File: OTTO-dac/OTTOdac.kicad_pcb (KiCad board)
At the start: 2 copper layers, 73 x 35 mm, 40 parts, among them J1 Conn_01x10, J2 Audio_IN, J3 Audio_OUT, J4 SJ1-42536-SMT, J5 Speaker, U1 AMS1117-3.3, U2 SGTL5000, U3 LM4860, X1 XO32

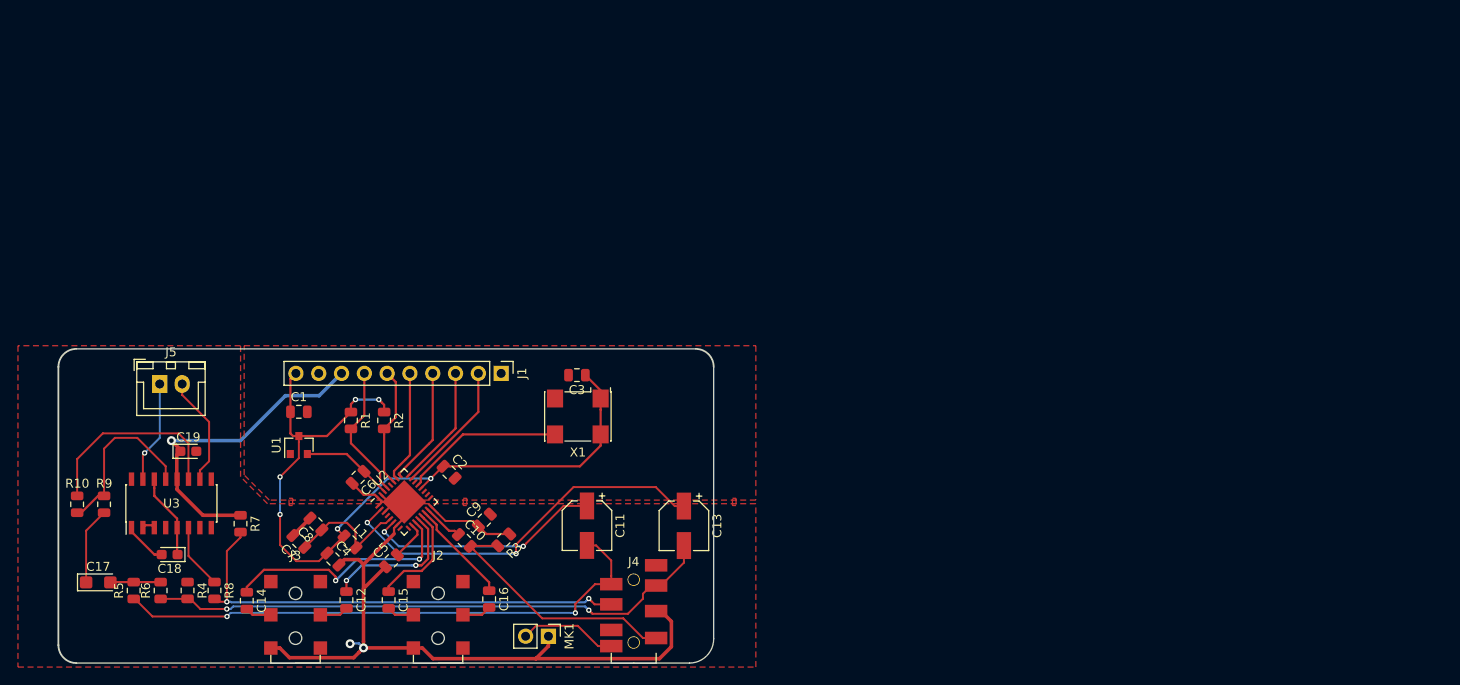
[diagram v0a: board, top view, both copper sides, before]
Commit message: new board, still needs gnd to be routed
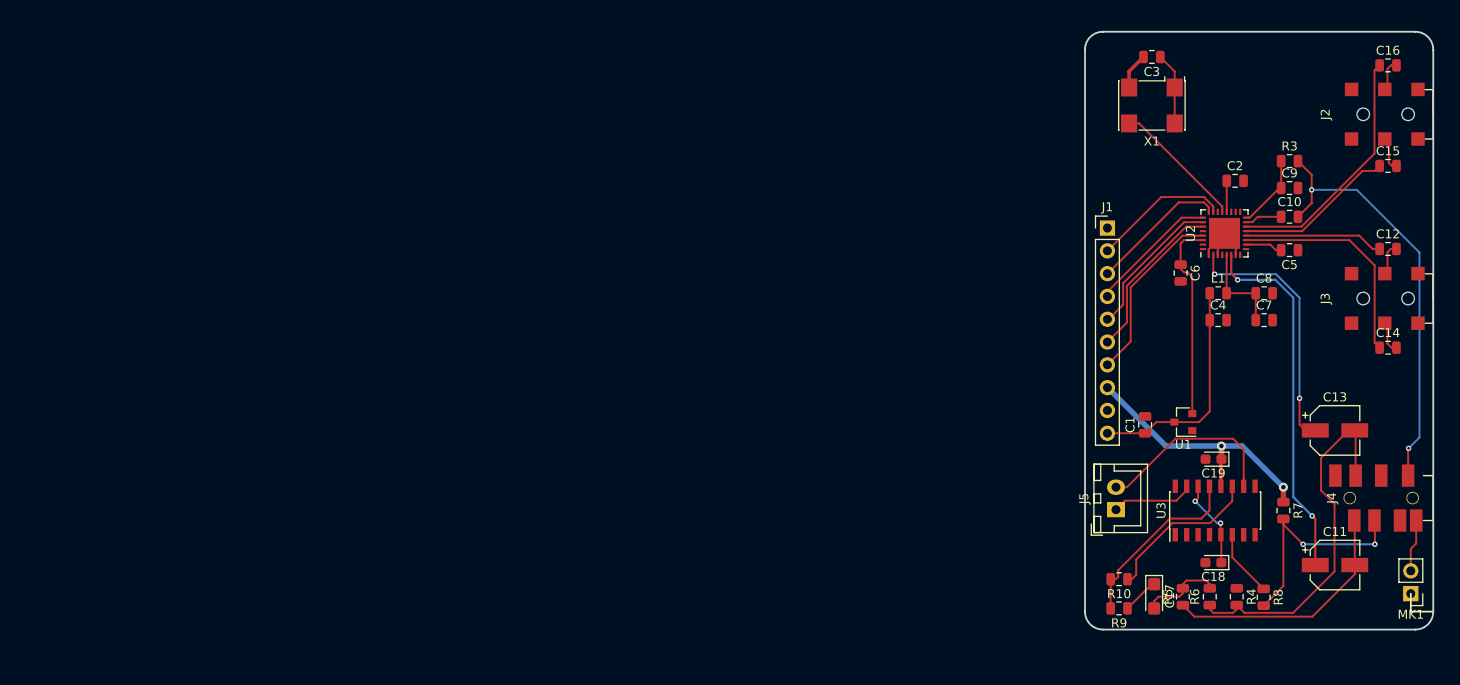
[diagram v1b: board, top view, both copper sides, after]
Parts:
- removed R1, R2: 2.2K, Resistor_SMD:R_0805_2012Metric
- moved C14 130.2 mm to (328.2, 118.6), turned to 0 degrees
- moved J3 128.1 mm to (329.2, 113.1), turned to 270 degrees
- moved C12 122.4 mm to (328.2, 107.6), turned to 0 degrees
- moved C15 121.4 mm to (328.2, 98.4), turned to 0 degrees
- moved J2 121.2 mm to (329.2, 92.6), turned to 270 degrees
- moved C17 117.6 mm to (302.1, 146.3), turned to 270 degrees
- moved R8 116.9 mm to (314.3, 146.4)
- moved R4 116.9 mm to (311.3, 146.4)
- moved R5 116.9 mm to (305.3, 146.4)
- moved R6 116.9 mm to (308.3, 146.4)
- moved C16 116.5 mm to (328.2, 87.2), turned to 0 degrees
- moved R10 116.4 mm to (298.2, 144.4), turned to 180 degrees
- moved C18 116.3 mm to (308.7, 142.6)
- moved U3 116.3 mm to (308.9, 136.8)
- moved R7 116.2 mm to (316.5, 136.8)
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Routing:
- net GNDREF: track 103.7 -> 9.25 mm, vias 2 -> 0
- net +3V3: track 87.1 -> 37.1 mm, vias 6 -> 0
- net HPL: track 62.0 -> 27.6 mm, vias 2 -> 0
- net Net-(J4-Pad6): track 53.2 -> 25.0 mm
- net HPR: track 63.5 -> 40.8 mm, vias 2 -> 0
- net MIC: track 28.0 -> 47.7 mm, vias 0 -> 2
- net Net-(C16-Pad1): track 11.7 -> 27.7 mm
- net Net-(C11-Pad1): track 26.7 -> 41.5 mm
- net Net-(C13-Pad1): track 43.4 -> 28.9 mm
- net Net-(C6-Pad1): track 10.1 -> 22.4 mm
- net Net-(J5-Pad2): track 12.3 -> 21.1 mm
- net +5V: track 36.3 -> 30.4 mm, vias 1 -> 2
- net Net-(C15-Pad1): track 12.2 -> 17.9 mm
- net Net-(J4-Pad8): track 11.0 -> 5.86 mm
- net PIN5: track 15.1 -> 20.1 mm
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- removed copper zone on F.Cu, net GNDREF
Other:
- board size 73 x 35 mm -> 38.8 x 66.6 mm

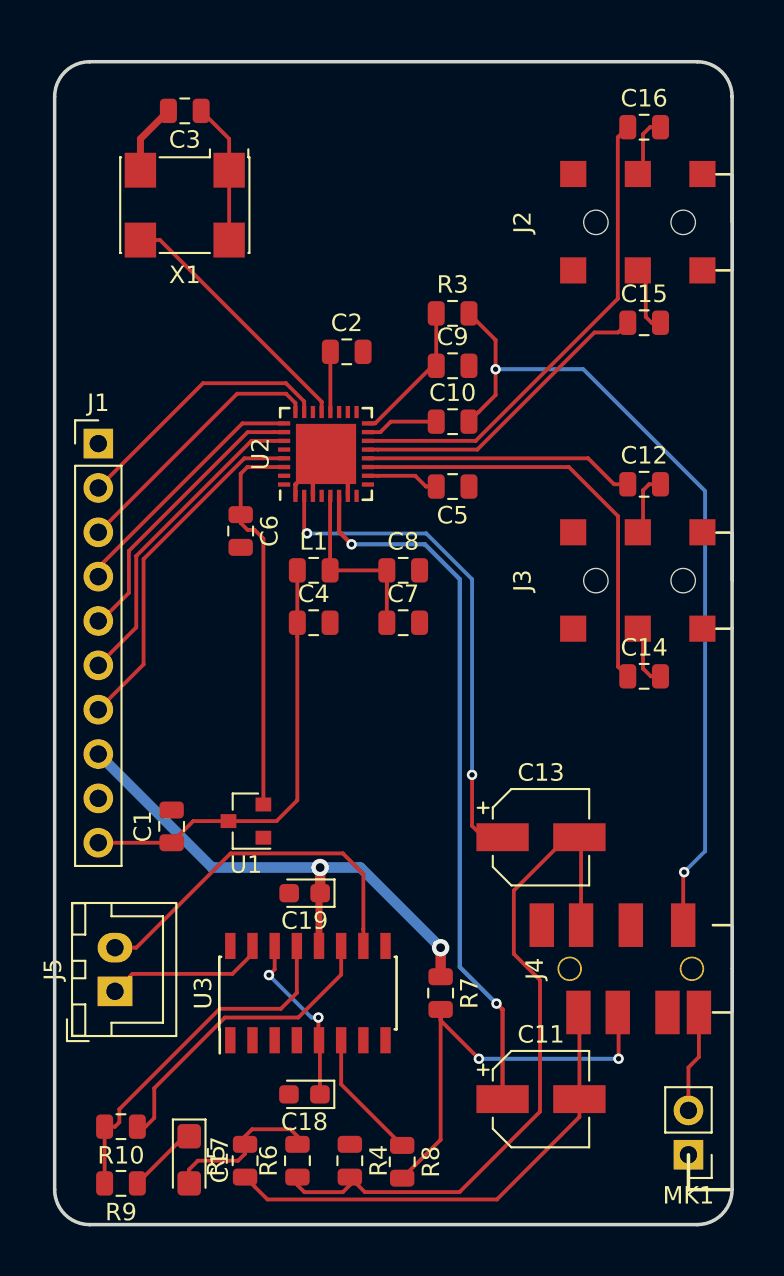
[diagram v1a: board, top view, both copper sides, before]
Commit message: routed ground and added mounting holes
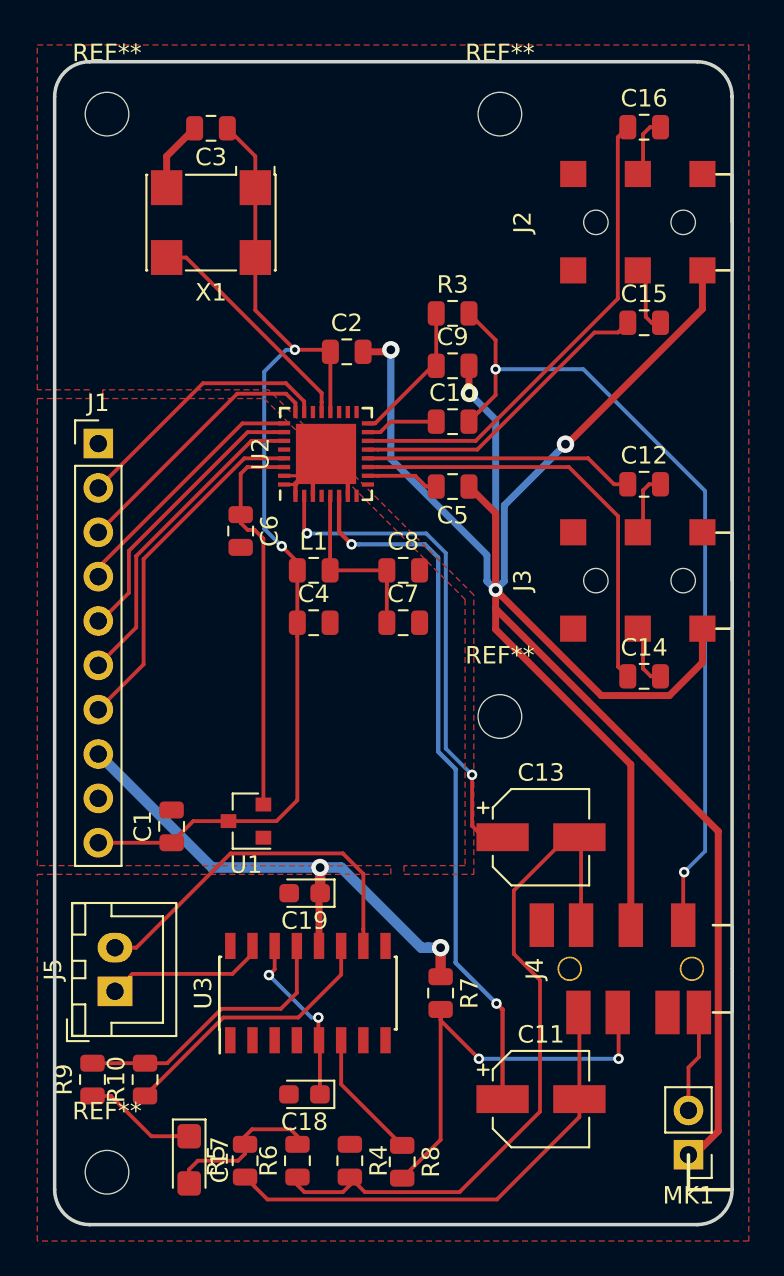
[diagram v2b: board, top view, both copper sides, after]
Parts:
- added REF**: MountingHole_2.5mm, MountingHole:MountingHole_2.5mm, F.Cu at (297.4, 147.0)
- added REF**: MountingHole_2.5mm, MountingHole:MountingHole_2.5mm, F.Cu at (319.9, 120.9)
- added REF**: MountingHole_2.5mm, MountingHole:MountingHole_2.5mm, F.Cu at (319.9, 86.4)
- added REF**: MountingHole_2.5mm, MountingHole:MountingHole_2.5mm, F.Cu at (297.4, 86.4)
- moved R9 6.17 mm to (296.6, 141.7), turned to 90 degrees
- moved R10 3.03 mm to (299.6, 141.7), turned to 90 degrees
- moved C3 1.80 mm to (303.4, 87.2)
- moved X1 1.80 mm to (303.4, 92.6)
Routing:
- net GNDREF: track 9.25 -> 157.9 mm, vias 0 -> 4
- net +3V3: track 37.1 -> 59.8 mm, vias 0 -> 2
- net Net-(R10-Pad2): track 20.6 -> 16.6 mm
- net Net-(C17-Pad1): track 4.09 -> 6.76 mm
- net Net-(R10-Pad1): track 17.9 -> 15.8 mm
- net Net-(U2-Pad21): track 14.8 -> 13.2 mm
- added copper zone on F.Cu, net GNDREF

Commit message: started working on the mainboard
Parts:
- moved MK1 1.30 mm to (329.4, 146.0)
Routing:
- net GNDREF: track 157.9 -> 159.2 mm
- net Net-(J4-Pad8): track 5.86 -> 6.40 mm
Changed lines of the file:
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@@
   (general
     (thickness 1.6)
-    (drawings 1356)
+    (drawings 1354)
     (tracks 304)
     (zones 0)
@@
     (pad_to_mask_clearance 0)
     (aux_axis_origin 0 0)
-    (grid_origin 294.428234 85.423074)
+    (grid_origin 329.428234 146.02262)
     (visible_elements 7FFFFFFF)
     (pcbplotparams
@@
   )
   (module Connector_PinHeader_2.54mm:PinHeader_1x02_P2.54mm_Vertical (layer F.Cu)
-    (at 330.726868 146.02262 180)
+    (at 329.428234 146.02262 180)
     (descr "Through hole straight pin header, 1x02, 2.54mm pitch, single row")
     (tags "Through hole pin header THT 1x02 2.54mm single row")
@@
   (gr_line (start 294.428234 86.423074) (end 296.928234 86.423074) (layer Cmts.User) (width 0.2))
   (gr_line (start 294.428234 85.423074) (end 294.428234 86.423074) (layer Cmts.User) (width 0.2))
-  (gr_line (start 330.726868 148.02262) (end 330.726868 146.02262) (layer F.SilkS) (width 0.2))
-  (gr_line (start 333.226868 148.02262) (end 330.726868 148.02262) (layer F.SilkS) (width 0.2))
   (gr_line (start 264.726868 169.58094) (end 274.726868 169.58094) (layer Cmts.User) (width 0.2))
   (gr_arc (start 273.726868 159.58094) (end 274.726868 159.58094) (angle -90) (layer Cmts.User) (width 0.2))
@@
   (segment (start 323.683869 105.326548) (end 320.183869 108.826548) (width 0.4) (layer B.Cu) (net 1))
   (segment (start 320.183869 108.826548) (end 320.183869 113.170762) (width 0.4) (layer B.Cu) (net 1))
-  (segment (start 328.183869 123.25) (end 319.683869 114.75) (width 0.4) (layer F.Cu) (net 1))
-  (segment (start 332.433869 127.5) (end 328.183869 123.25) (width 0.4) (layer F.Cu) (net 1))
-  (segment (start 332.433869 144.670782) (end 332.433869 127.5) (width 0.4) (layer F.Cu) (net 1))
-  (segment (start 330.726868 146.02262) (end 331.082031 146.02262) (width 0.4) (layer F.Cu) (net 1))
-  (segment (start 331.082031 146.02262) (end 332.433869 144.670782) (width 0.4) (layer F.Cu) (net 1))
   (segment (start 308.719713 107.136548) (end 309.107213 106.749048) (width 0.18) (layer F.Cu) (net 1))
   (segment (start 307.569713 107.136548) (end 308.719713 107.136548) (width 0.18) (layer F.Cu) (net 1))
@@
   (segment (start 310.832213 105.024048) (end 310.832213 106.749048) (width 0.18) (layer F.Cu) (net 1))
   (segment (start 309.107213 106.749048) (end 310.832213 106.749048) (width 0.18) (layer F.Cu) (net 1))
+  (segment (start 328.183869 123.25) (end 319.683869 114.75) (width 0.4) (layer F.Cu) (net 1))
+  (segment (start 332.433869 127.5) (end 328.183869 123.25) (width 0.4) (layer F.Cu) (net 1))
+  (segment (start 332.433869 144.670782) (end 332.433869 127.5) (width 0.4) (layer F.Cu) (net 1))
+  (segment (start 329.428234 146.023074) (end 331.081577 146.023074) (width 0.4) (layer F.Cu) (net 1))
+  (segment (start 331.081577 146.023074) (end 332.433869 144.670782) (width 0.4) (layer F.Cu) (net 1))
   (segment (start 309.568868 131.105259) (end 309.633869 131.040258) (width 0.4) (layer F.Cu) (net 2))
   (segment (start 309.568868 134.062757) (end 309.568868 131.105259) (width 0.4) (layer F.Cu) (net 2))
@@
   (segment (start 326.726868 137.92263) (end 326.676708 137.87247) (width 0.22) (layer F.Cu) (net 32))
   (segment (start 326.726868 140.52262) (end 326.726868 137.92263) (width 0.22) (layer F.Cu) (net 32))
-  (segment (start 330.726868 143.48262) (end 330.726868 141.02262) (width 0.22) (layer F.Cu) (net 34))
-  (segment (start 331.326708 140.42278) (end 331.326708 137.87247) (width 0.22) (layer F.Cu) (net 34))
-  (segment (start 330.726868 141.02262) (end 331.326708 140.42278) (width 0.22) (layer F.Cu) (net 34))
+  (segment (start 329.428234 142.321254) (end 329.428234 143.48262) (width 0.22) (layer F.Cu) (net 34))
+  (segment (start 331.326708 137.87247) (end 331.326708 140.42278) (width 0.22) (layer F.Cu) (net 34))
+  (segment (start 331.326708 140.42278) (end 329.428234 142.321254) (width 0.22) (layer F.Cu) (net 34))
   (segment (start 312.108868 133.092757) (end 312.108868 134.062757) (width 0.22) (layer F.Cu) (net 35))
   (segment (start 312.108868 129.937757) (end 312.108868 133.092757) (width 0.22) (layer F.Cu) (net 35))
@@
         (xy 326.933869 131.170782) (xy 326.183869 131.170782) (xy 326.183869 134.670782) (xy 328.683869 134.670782) (xy 328.683869 131.170782)
         (xy 327.933869 131.170782) (xy 327.933869 124.670782) (xy 328.433869 124.170782) (xy 331.933869 127.670782) (xy 331.933869 144.420782)
-        (xy 331.683869 144.670782) (xy 329.183869 144.670782) (xy 329.183869 147.420782) (xy 332.183869 147.420782) (xy 332.183869 145.670782)
+        (xy 331.683869 144.670782) (xy 327.928234 144.673074) (xy 327.928234 147.423074) (xy 330.928234 147.423074) (xy 330.928234 146.923074)
         (xy 333.183869 144.670782) (xy 333.183869 127.420782) (xy 326.683869 120.920782) (xy 327.433869 120.170782) (xy 329.933869 120.170782)
         (xy 332.183869 117.920782) (xy 332.183869 117.170782) (xy 332.683869 117.170782) (xy 332.683869 114.670782) (xy 330.183869 114.670782)
